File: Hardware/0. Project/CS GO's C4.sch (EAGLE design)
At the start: 46 parts, among them CN1 CELL--PHMC4-02, CN2 ICSP, CN4 TERMINAL-BLOCK-2P-5MM, CN5 TERMINAL-BLOCK-2P-5MM, Q1 NPN-BC817, Q3 N-FET-ENHANCEMENT-SQ2310, Q5 N-FET-ENHANCEMENT-SQ2310, U1 1117-3.3V, U3 1117-3.3V, U4 PCF8574DW, U6 ATMEGA328P-AU, Y1 16 MHz

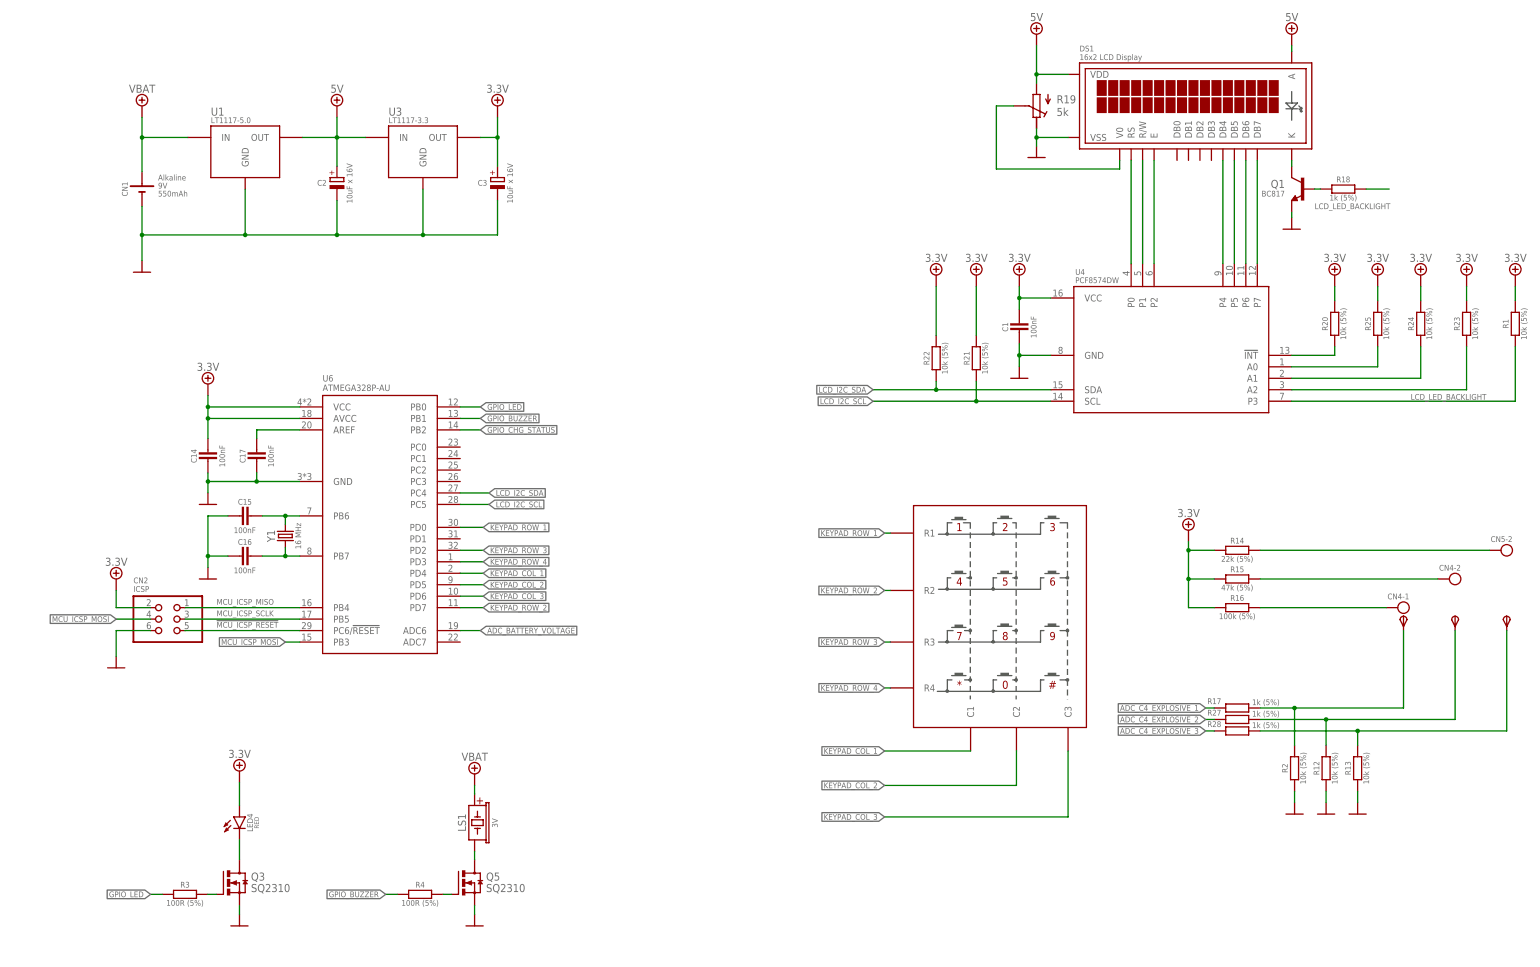
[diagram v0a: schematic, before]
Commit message: added pull down at buzzer and LED drivers
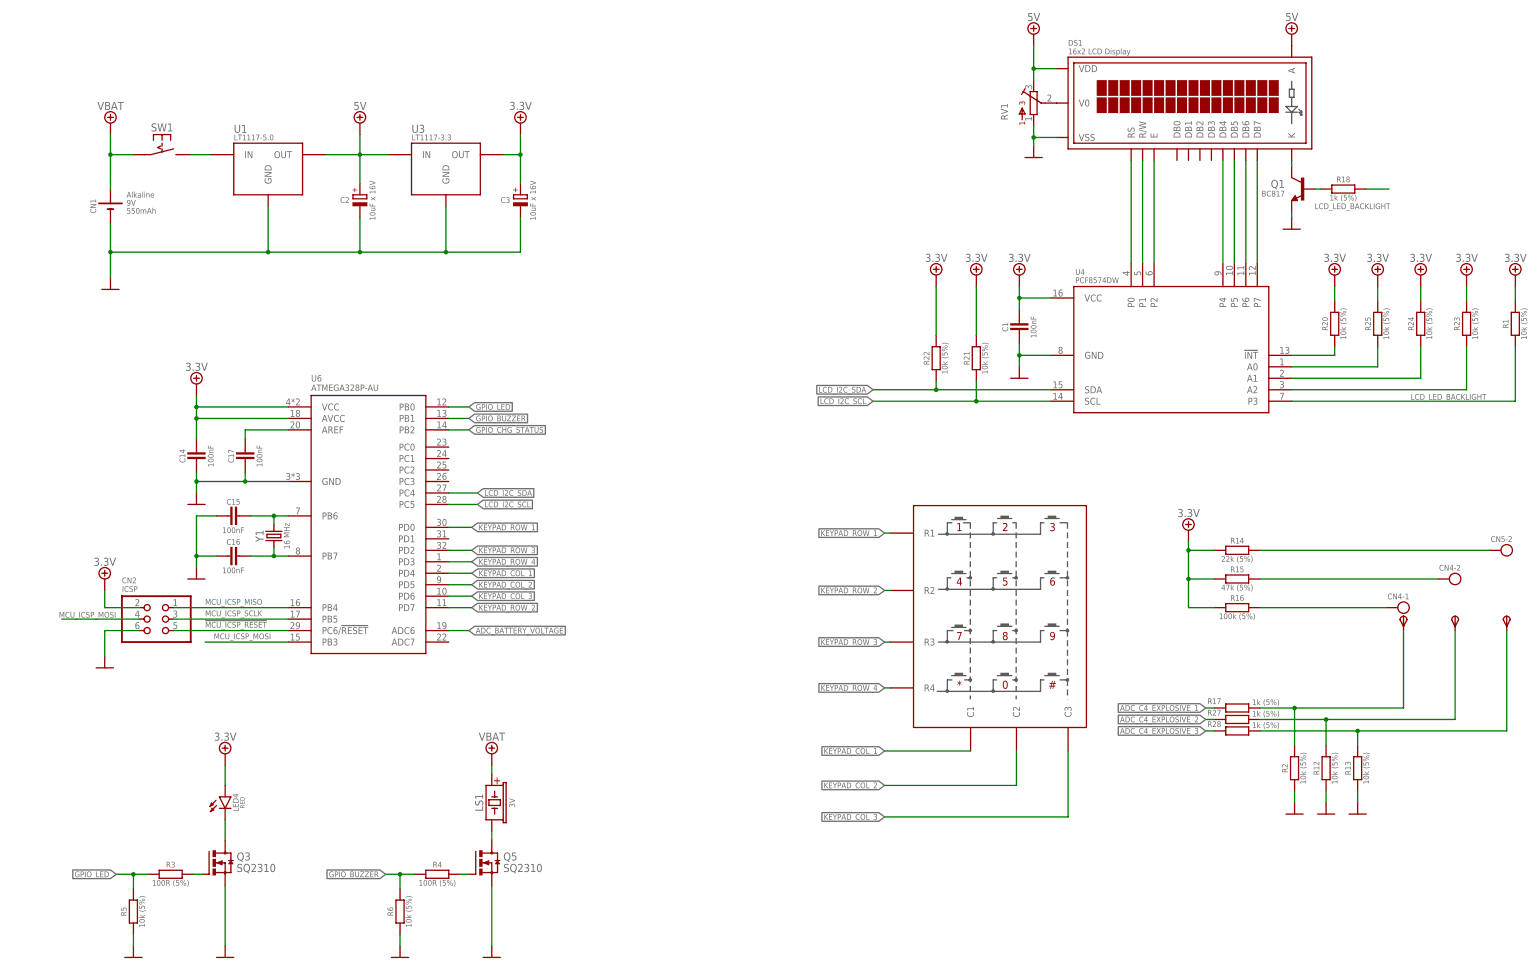
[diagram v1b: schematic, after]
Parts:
- removed R19: 5k, trimpot-molex2p:R-TRIMM
- added R5, R6: 10k (5%), My-RLC:R_0603
- added RV1: (no value), My-RLC:RV_F
- added SW1: SPST-LATCH-PHMC4-02, My-Switches:SPST-LATCH-PHMC4-02
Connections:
- removed net N$34: DS1.V0, R19.S
- new net N$10: SW1.SW2, U1.IN
- new net N$13: DS1.V0, RV1.2
- net 0V: now also R5.1, R6.1, RV1.1; no longer R19.E
- net 5.0V: now also RV1.3; no longer R19.A
- net GPIO_BUZZER: now also R6.2
- net GPIO_LED: now also R5.2
- net P$1: now also SW1.SW1; no longer U1.IN
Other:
- moved on the sheet: C14, C15, C16, C17, C2, C3, CN1, CN2, LED4, LS1, Q3, Q5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

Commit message: added C4 shells detection ADC pins to MCU
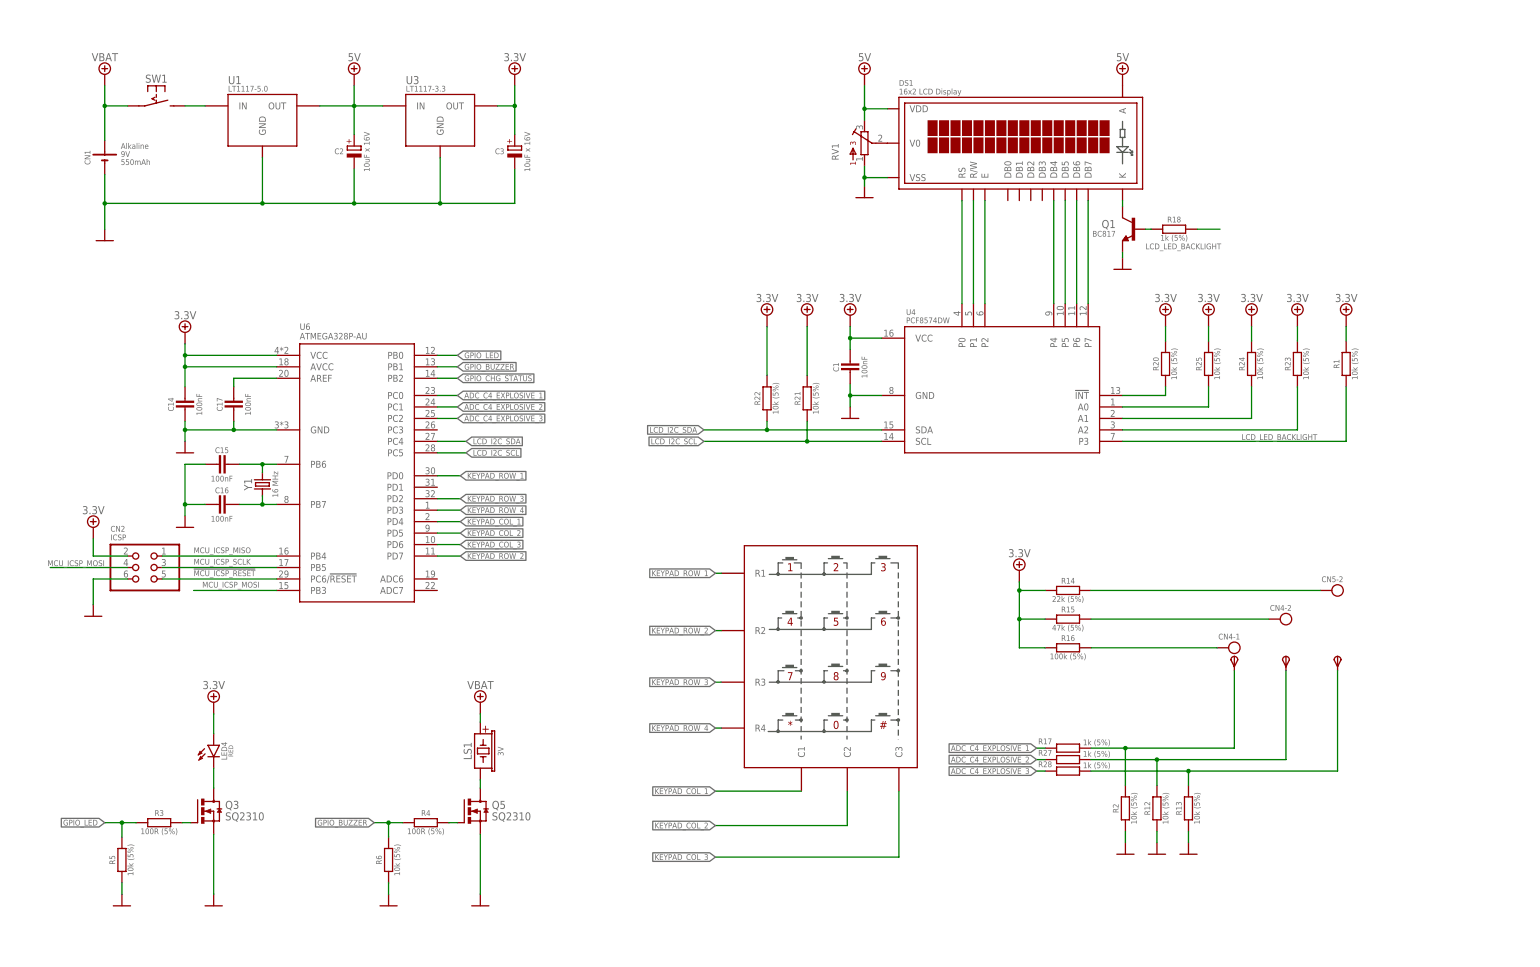
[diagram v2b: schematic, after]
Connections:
- removed net ADC_BATTERY_VOLTAGE: U6.ADC6
- net ADC_C4_EXPLOSIVE_1: now also U6.PC0
- net ADC_C4_EXPLOSIVE_2: now also U6.PC1
- net ADC_C4_EXPLOSIVE_3: now also U6.PC2
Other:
- moved on the sheet: C1, C14, C15, C16, C17, C2, C3, CN1, CN2, CN4-1, CN4-2, CN5-2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

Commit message: fixed VOUT value of C4 shell voltage dividers
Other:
- note added: "0.30V"
- note added: "0.57V"
- note added: "1.00V"
- note removed: "0.59V"
- note removed: "1.05V"
- note removed: "1.64V"
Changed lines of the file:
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@@
 <attribute name="AUTHOR" value="Tiago Silva"/>
 <attribute name="SOURCE" value="github.com/TiagoPaulaSilva/CS-GO-s-C4"/>
-<attribute name="VERSION" value="1.2"/>
+<attribute name="VERSION" value="1.3"/>
 </attributes>
 <variantdefs>
@@
 <rectangle x1="308.61" y1="86.36" x2="342.9" y2="89.535" layer="135" grouprefs="C4_SHELLS_DETECTION"/>
 <rectangle x1="308.61" y1="54.61" x2="342.9" y2="57.785" layer="135" grouprefs="C4_SHELLS_DETECTION"/>
-<text x="290.195" y="78.105" size="1.27" layer="137" font="vector" ratio="10" align="center" grouprefs="C4_SHELLS_DETECTION">1.64V</text>
-<text x="297.18" y="75.565" size="1.27" layer="137" font="vector" ratio="10" align="center" grouprefs="C4_SHELLS_DETECTION">1.05V</text>
-<text x="304.165" y="73.025" size="1.27" layer="137" font="vector" ratio="10" align="center" grouprefs="C4_SHELLS_DETECTION">0.59V</text>
+<text x="290.195" y="78.105" size="1.27" layer="137" font="vector" ratio="10" align="center" grouprefs="C4_SHELLS_DETECTION">0.30V</text>
+<text x="297.18" y="75.565" size="1.27" layer="137" font="vector" ratio="10" align="center" grouprefs="C4_SHELLS_DETECTION">0.57V</text>
+<text x="304.165" y="73.025" size="1.27" layer="137" font="vector" ratio="10" align="center" grouprefs="C4_SHELLS_DETECTION">1.00V</text>
 <text x="294.64" y="100.965" size="1.778" layer="140" font="vector" ratio="15" rot="R180" align="center" grouprefs="C4_SHELLS_DETECTION">RED WIRE</text>
 <text x="294.64" y="106.68" size="1.778" layer="135" font="vector" ratio="15" rot="R180" align="center" grouprefs="C4_SHELLS_DETECTION">BLACK WIRE</text>

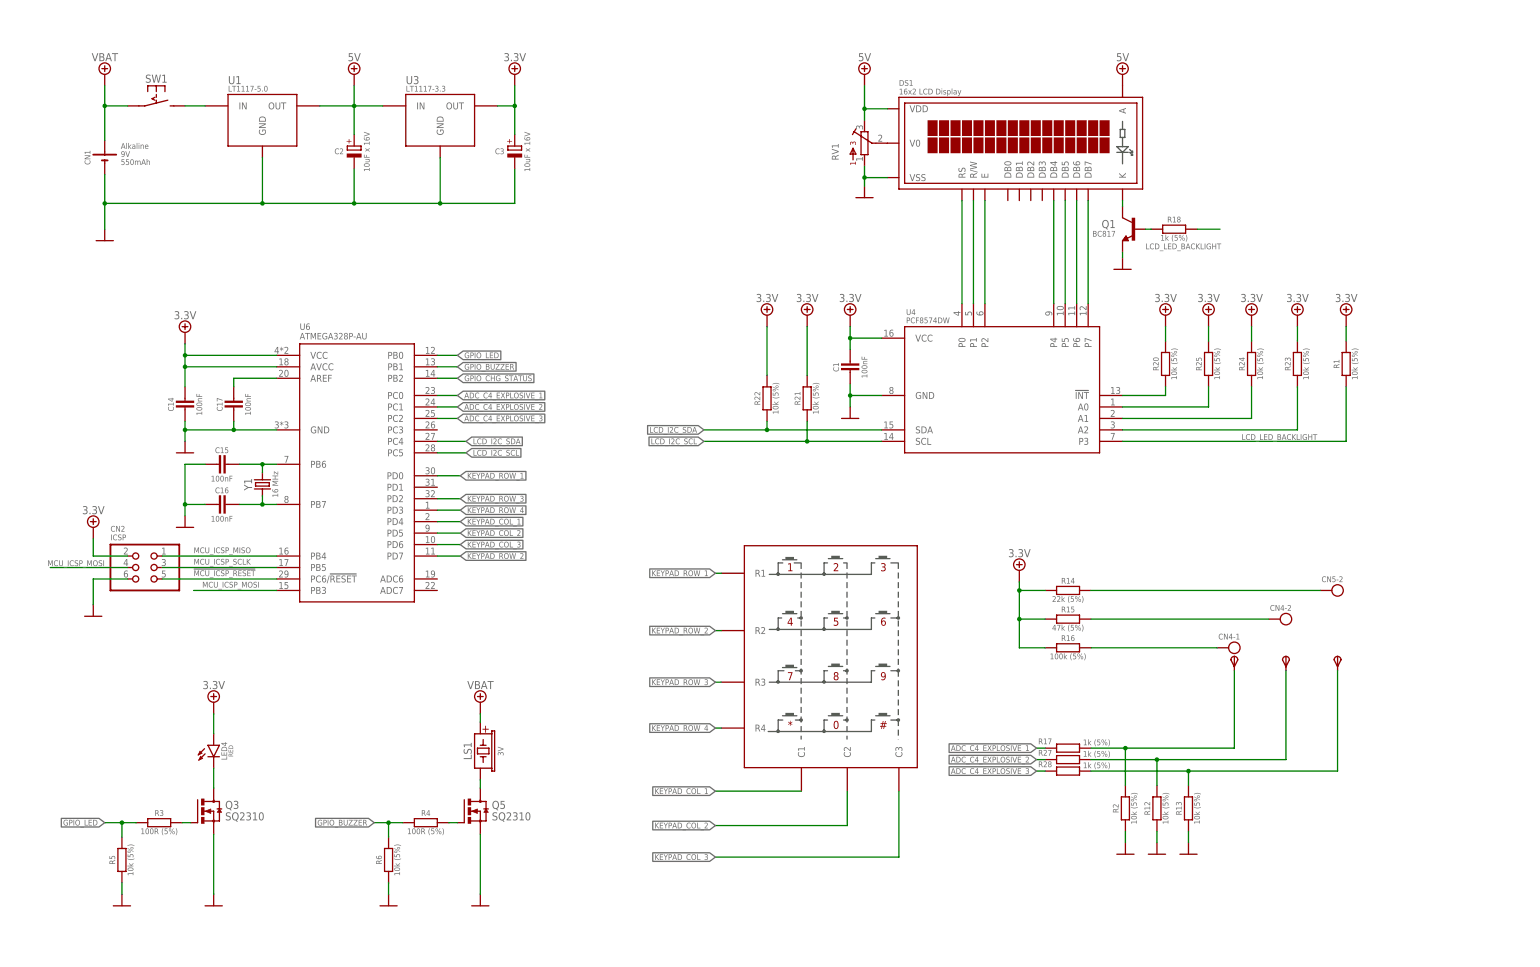
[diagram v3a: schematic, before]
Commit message: Changes MCU to PTH version and supply to 5V
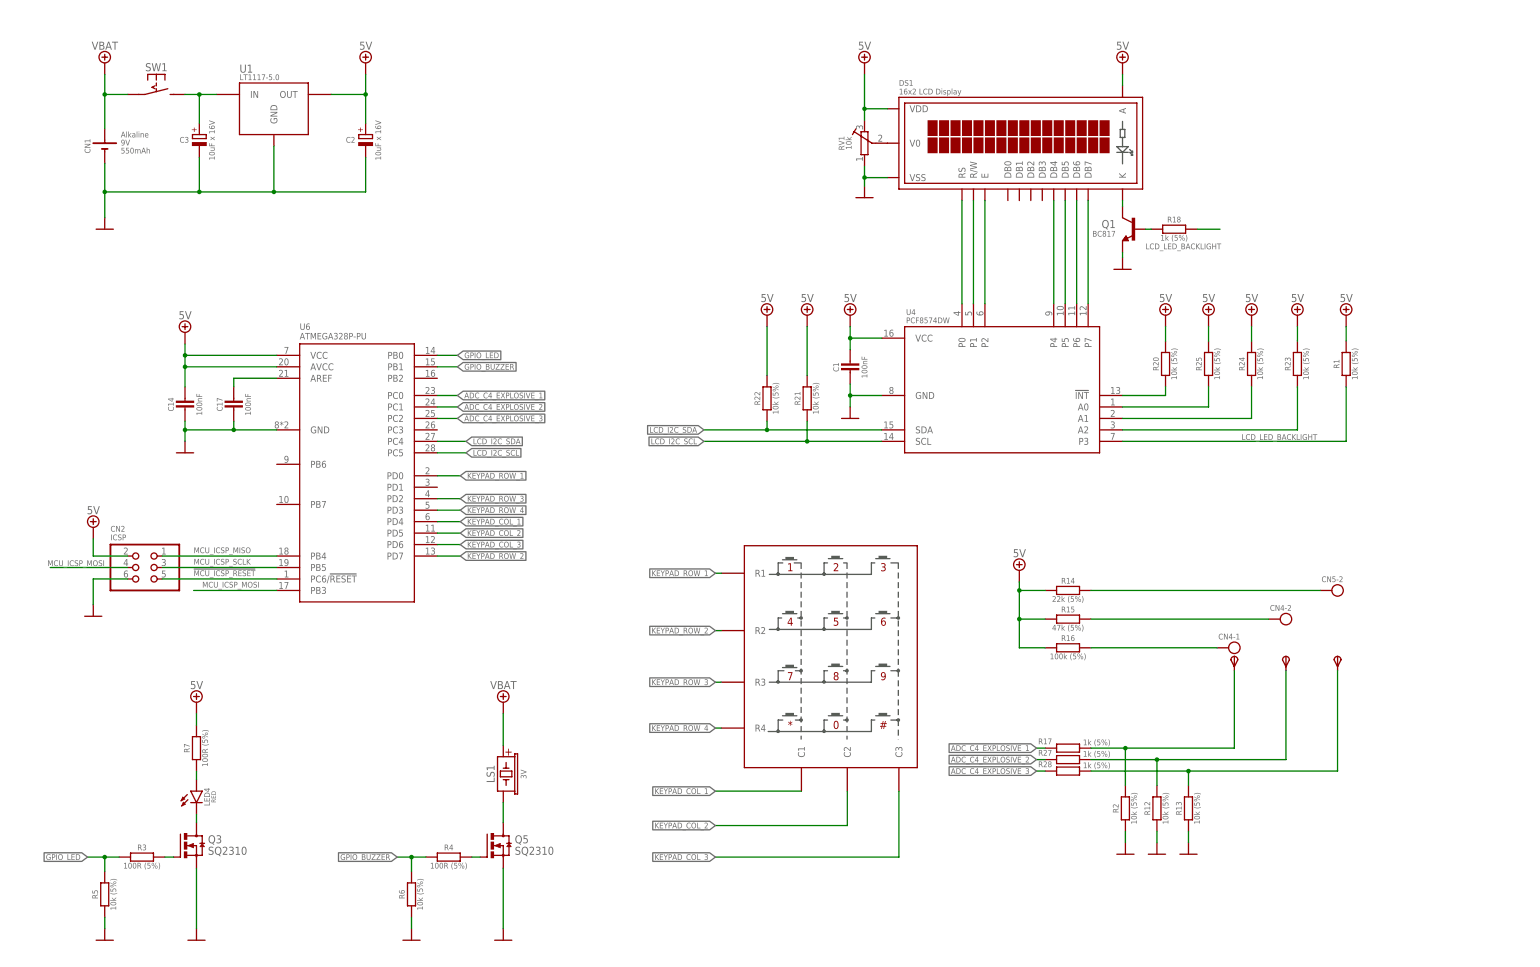
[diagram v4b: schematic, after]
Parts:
- removed C15, C16: 100nF, My-RLC:C_0603
- removed U3: 1117-3.3V, My-LDOs:1117-3.3V
- removed Y1: 16 MHz, My-Crystals:OSC-32.768KHZ
- added R7: 100R (5%), My-RLC:R_0603
- RV1: value (none) -> 10k
- U6: value ATMEGA328P-AU -> ATMEGA328P-PU; device My-Microcontrollers:ATMEGA328P-AU -> My-Microcontrollers:ATMEGA328P-PU
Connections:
- removed net 3.3V: C1.1, C14.1, C3.+, CN2.2, LED4.A, R1.2, R14.1, R15.1, R16.1, R20.2, R21.2, R22.2, R23.2, R24.2, R25.2, U3.OUT, U4.VCC, U6.AVCC, U6.VCC
- removed net GPIO_CHG_STATUS: U6.PB2
- removed net N$12: C15.1, U6.PB6, Y1.2
- net 0V: no longer C15.2, C16.2, U3.GND
- net 5.0V: now also C1.1, C14.1, CN2.2, R1.2, R14.1, R15.1, R16.1, R20.2, R21.2, R22.2, R23.2, R24.2, R25.2, R7.2, U4.VCC, U6.AVCC, U6.VCC; no longer U3.IN
- net N$10: now also C3.+
- net N$9: now also LED4.A, R7.1; no longer C16.1, U6.PB7, Y1.1
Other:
- note added: "** needs custom bootloader ** checks Firmware\\CUSTOM\\README.txt"
- note removed: "0.30V"
- note removed: "0.57V"
- note removed: "1.00V"
- moved on the sheet: C2, C3, CN1, LED4, LS1, Q3, Q5, R3, R4, R5, R6, SW1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

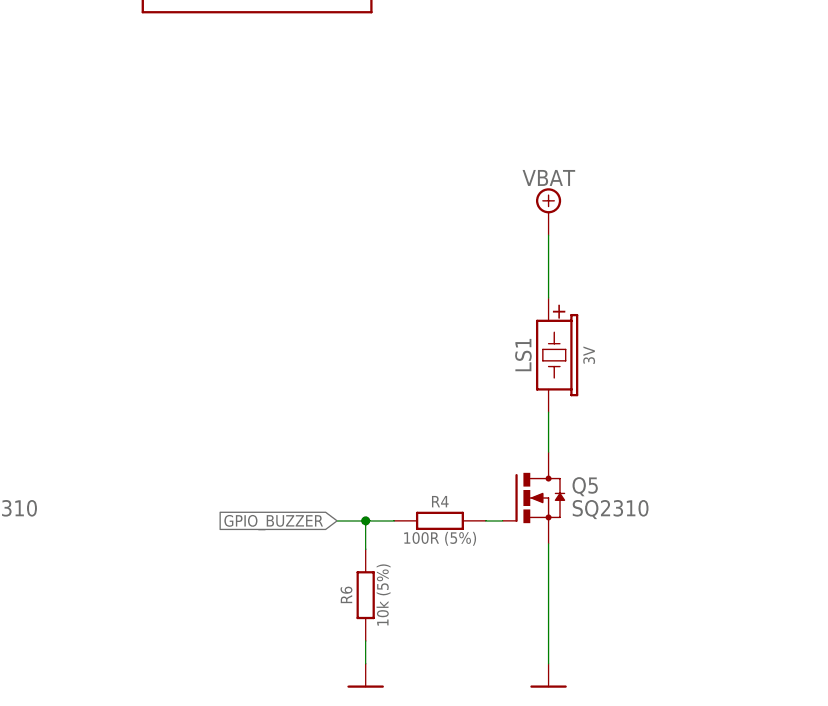
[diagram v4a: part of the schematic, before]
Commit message: remove piezo driver
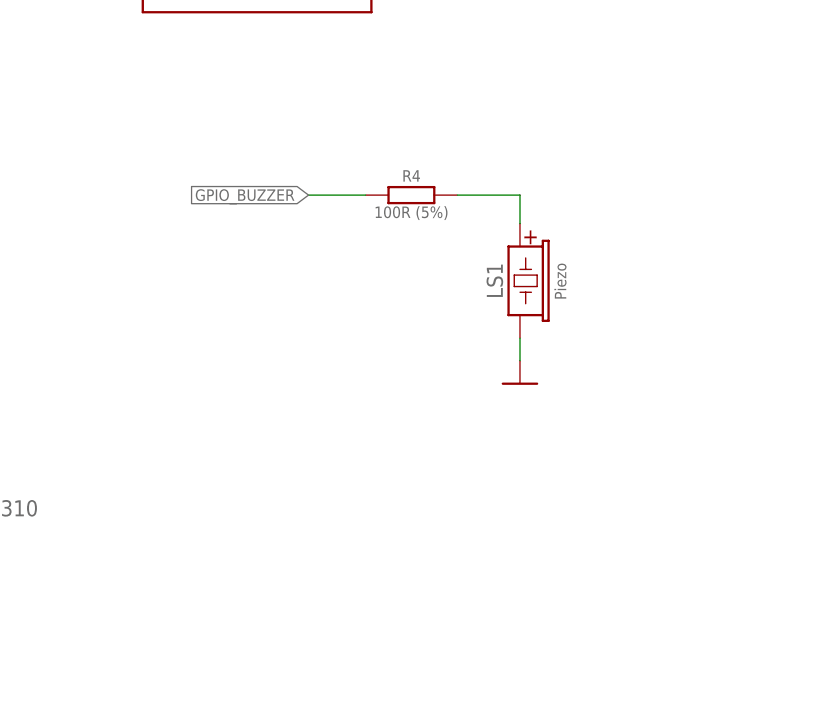
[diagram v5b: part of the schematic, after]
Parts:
- removed Q5: N-FET-ENHANCEMENT-SQ2310, My-Transistors:N-FET-ENHANCEMENT-SQ2310
- removed R6: 10k (5%), My-RLC:R_0603
- LS1: value 3V -> Piezo; FAMILY 3V -> Piezo
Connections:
- removed net N$6: Q5.G, R4.2
- net 0V: now also LS1.-; no longer Q5.S, R6.1
- net GPIO_BUZZER: no longer R6.2
- net N$1: now also LS1.+, R4.2; no longer LS1.-, Q5.D
- net P$1: no longer LS1.+
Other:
- moved on the sheet: LS1, R4
